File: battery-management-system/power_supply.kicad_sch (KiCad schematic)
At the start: 39 parts, among them J14 VIN, J24 3V3, J25 5V, J26 5V, U1 L6982C33DR, U12 MIC2250-1YD5, U2 L6982C33DR

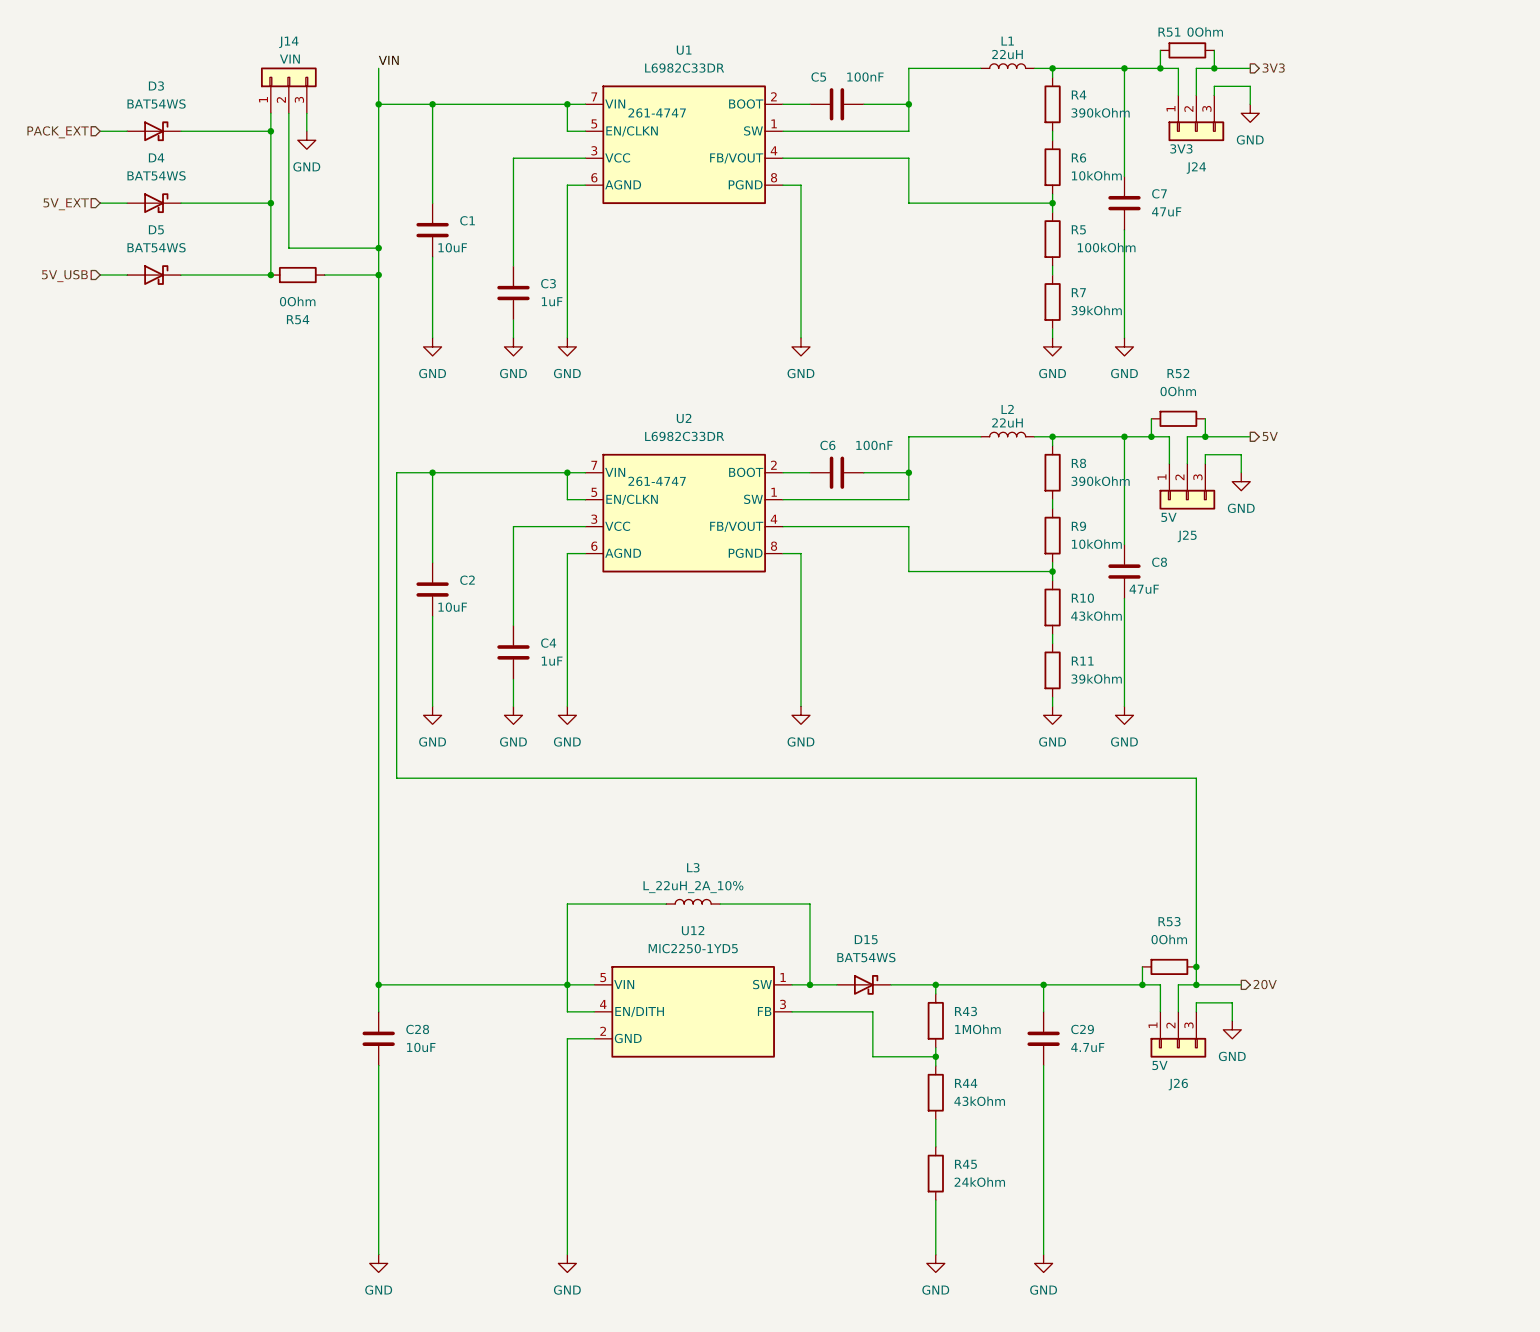
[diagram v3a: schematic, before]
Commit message: fix current sensing
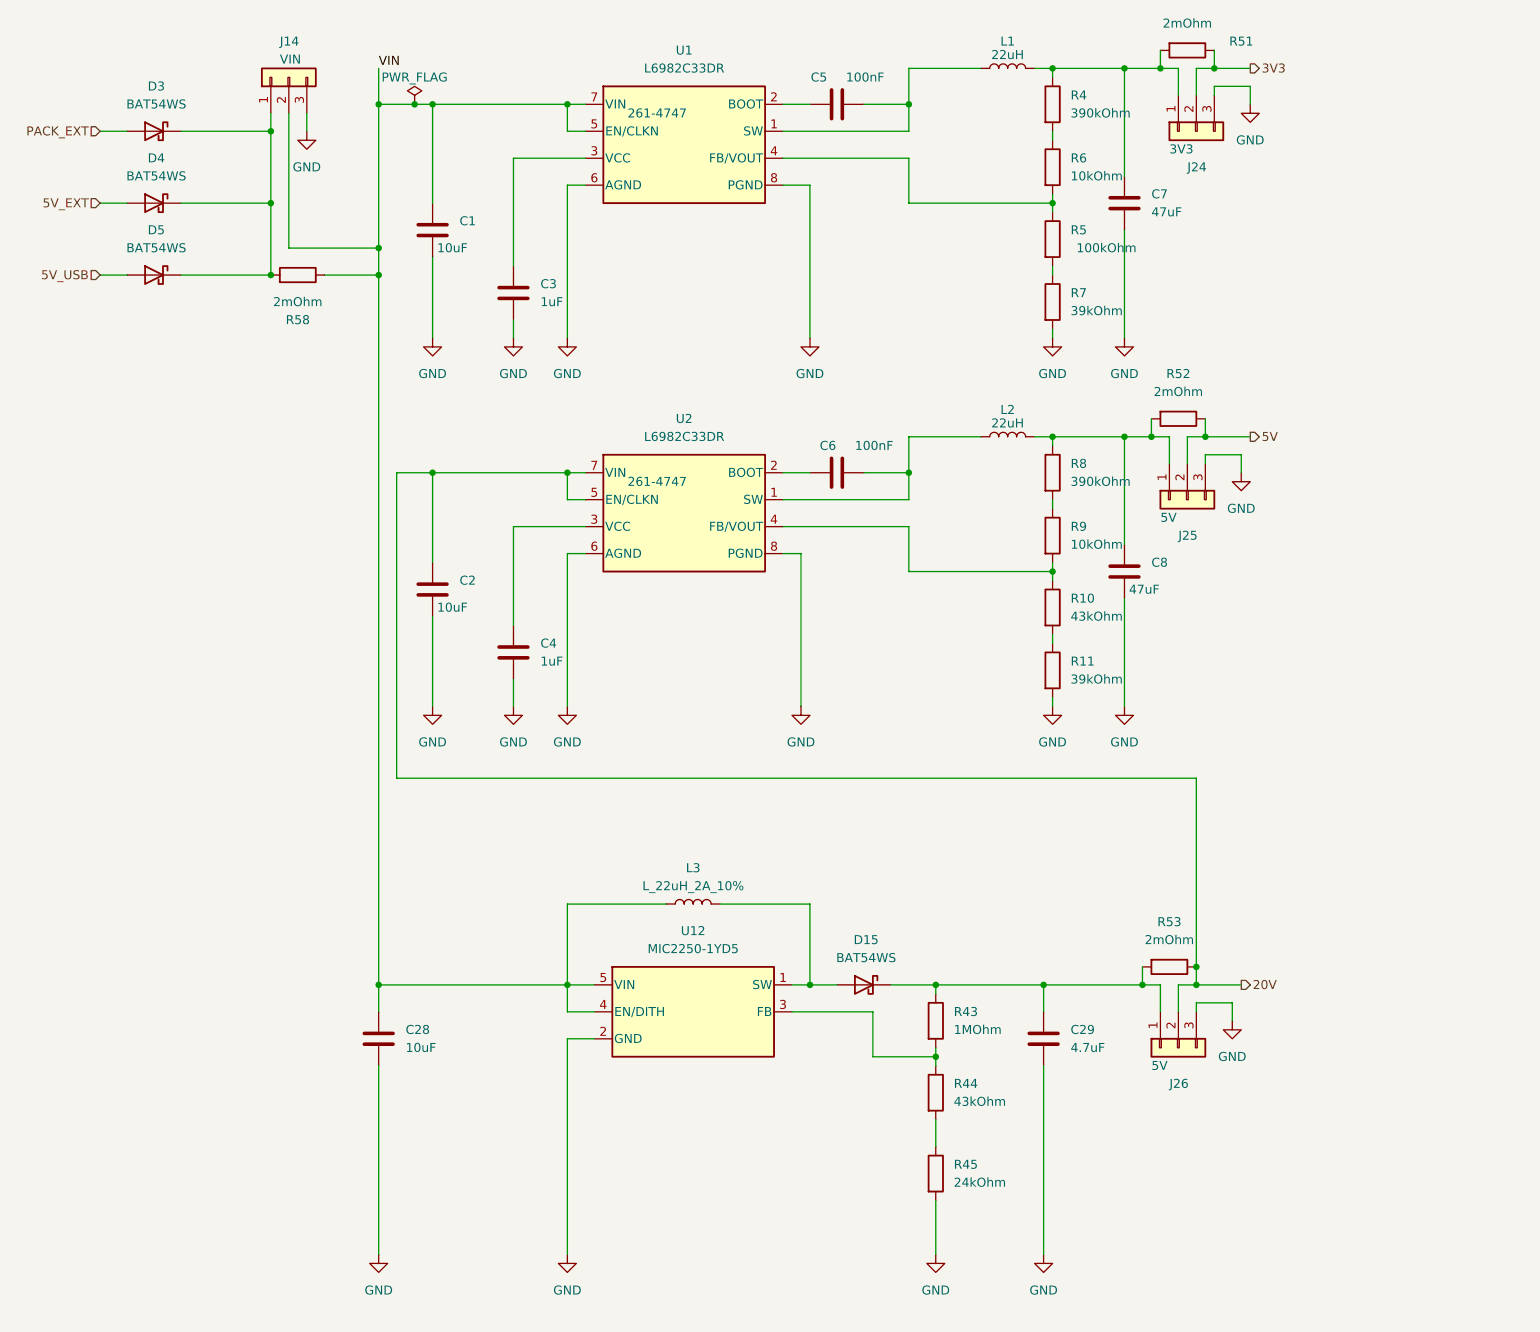
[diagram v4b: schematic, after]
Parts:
- removed R51, R52, R53, R54: 0Ohm, benediktibk:R_0603_1608Metric_Pad0.98x0.95mm_HandSolder, symbol benediktibk:R_0Ohm_SMD_0603_100mW_0%
- added R51, R52, R53, R58: 2mOhm, benediktibk:R_2512_6332Metric_Pad1.40x3.35mm_HandSolder, symbol benediktibk:R_2mOhm_SMD_2512_5W_1%
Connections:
- net 20V: now also R53.1
- net 3V3: now also R51.1
- net 5V: now also R52.1
- net VIN: now also R58.1
- net at C7.1, J24.1 (Pin_1), L1.1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: now also R51.2
- net at C8.1, J25.1 (Pin_1), L2.1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: now also R52.2
- net at C29.1, D15.1 (K), J26.1 (Pin_1)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: now also R53.2
- net at D3.1 (K), D4.1 (K), D5.1 (K)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: now also R58.2

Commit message: add negative power supply for OPAMPs
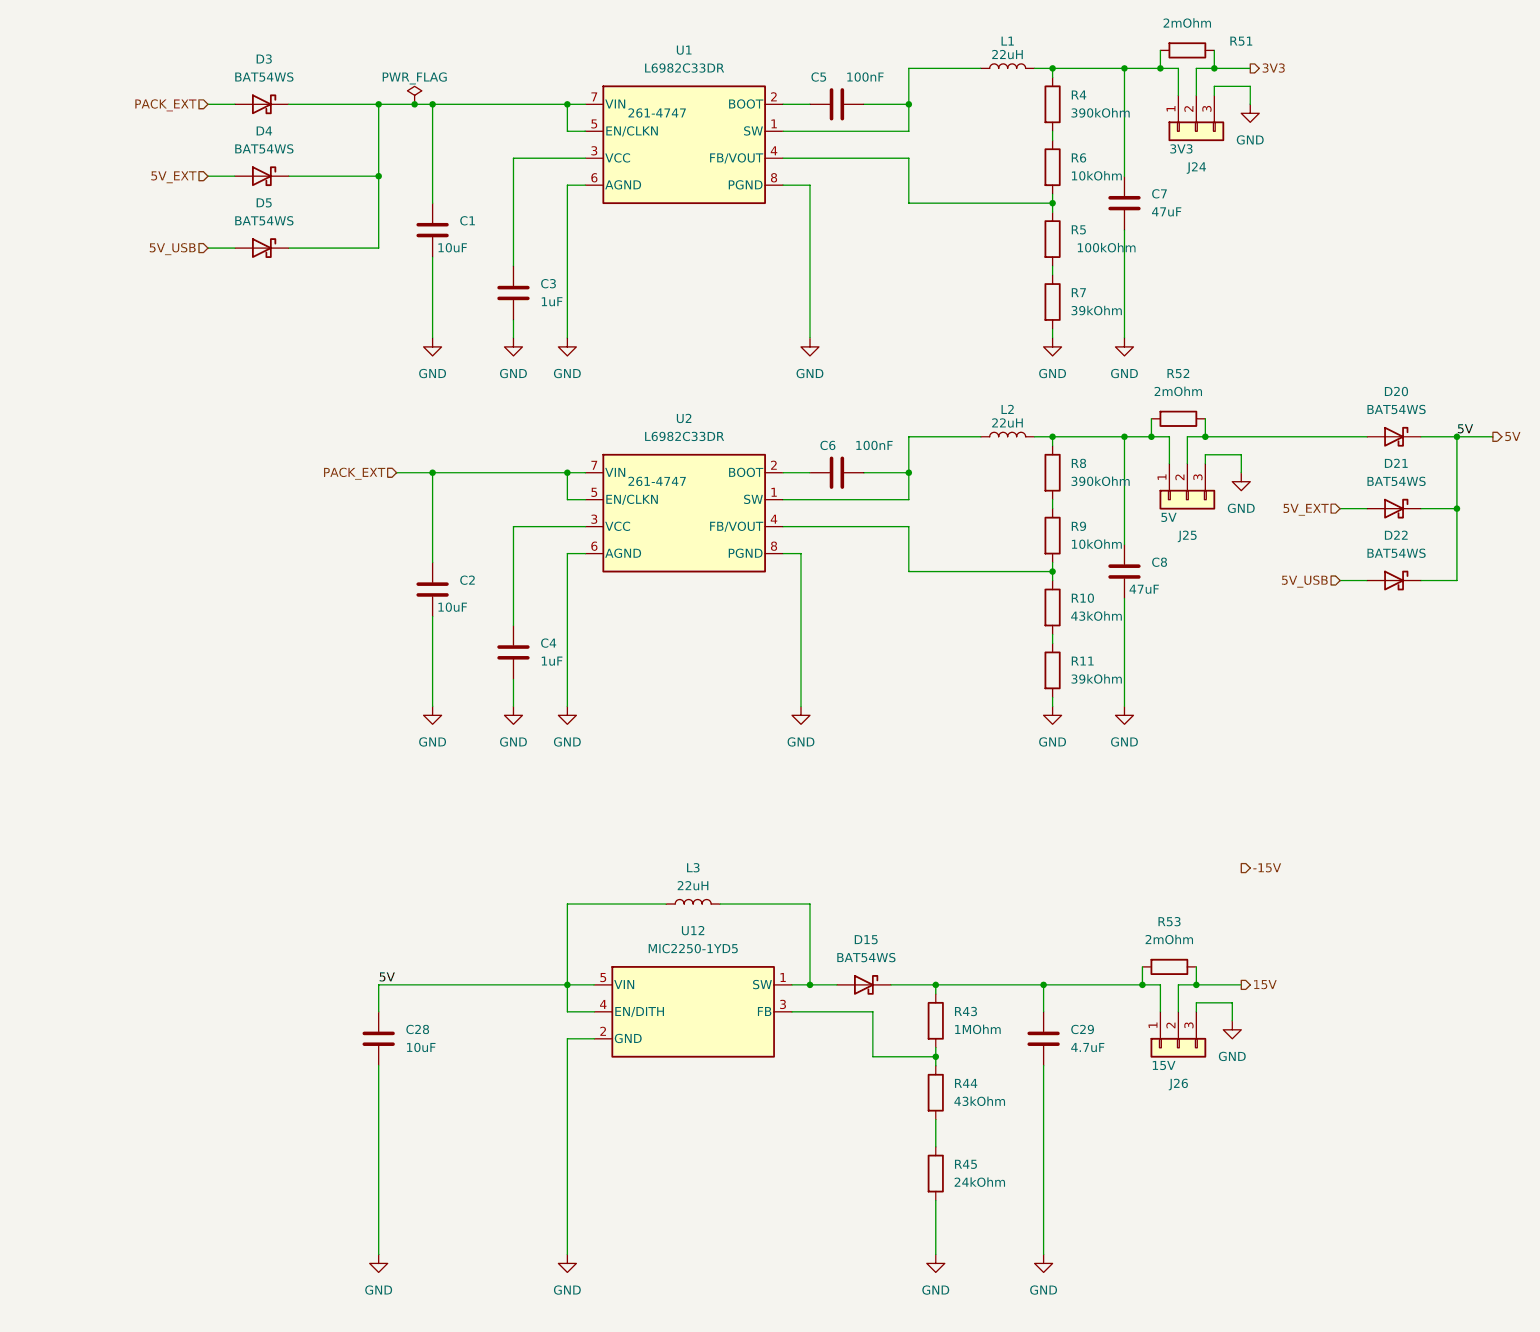
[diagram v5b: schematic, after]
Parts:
- removed J14: VIN, benediktibk:PinHeader_1x03_P2.54mm_Vertical, symbol benediktibk:Conn_01x03
- removed R58: 2mOhm, benediktibk:R_2512_6332Metric_Pad1.40x3.35mm_HandSolder, symbol benediktibk:R_2mOhm_SMD_2512_5W_1%
- added D20, D21, D22: BAT54WS, benediktibk:D_SOD-323, symbol benediktibk:BAT54WS
- J26: value 5V -> 15V
- L3: value L_22uH_2A_10% -> 22uH
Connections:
- net 5V: now also C28.1, L3.1, U12.4 (EN/DITH), U12.5 (VIN), D20.1 (K), D21.1 (K), D22.1 (K); no longer J25.2 (Pin_2), R52.1
- net 5V_EXT: now also D21.2 (A)
- net 5V_USB: now also D22.2 (A)
- net PACK_EXT: now also C2.1, U2.5 (EN/CLKN), U2.7 (VIN)
- net at D3.1 (K), D4.1 (K), D5.1 (K): now also C1.1, U1.5 (EN/CLKN), U1.7 (VIN)
- removed net 20V: C2.1, J26.2 (Pin_2), R53.1, U2.5 (EN/CLKN), U2.7 (VIN)
- removed net VIN: C1.1, C28.1, L3.1, U1.5 (EN/CLKN), U1.7 (VIN), U12.4 (EN/DITH), U12.5 (VIN)
- new net: D20.2 (A), J25.2 (Pin_2), R52.1
- new net 15V: J26.2 (Pin_2), R53.1
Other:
- moved on the sheet: D3, D4, D5

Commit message: implement negative power supply for OPAMPs
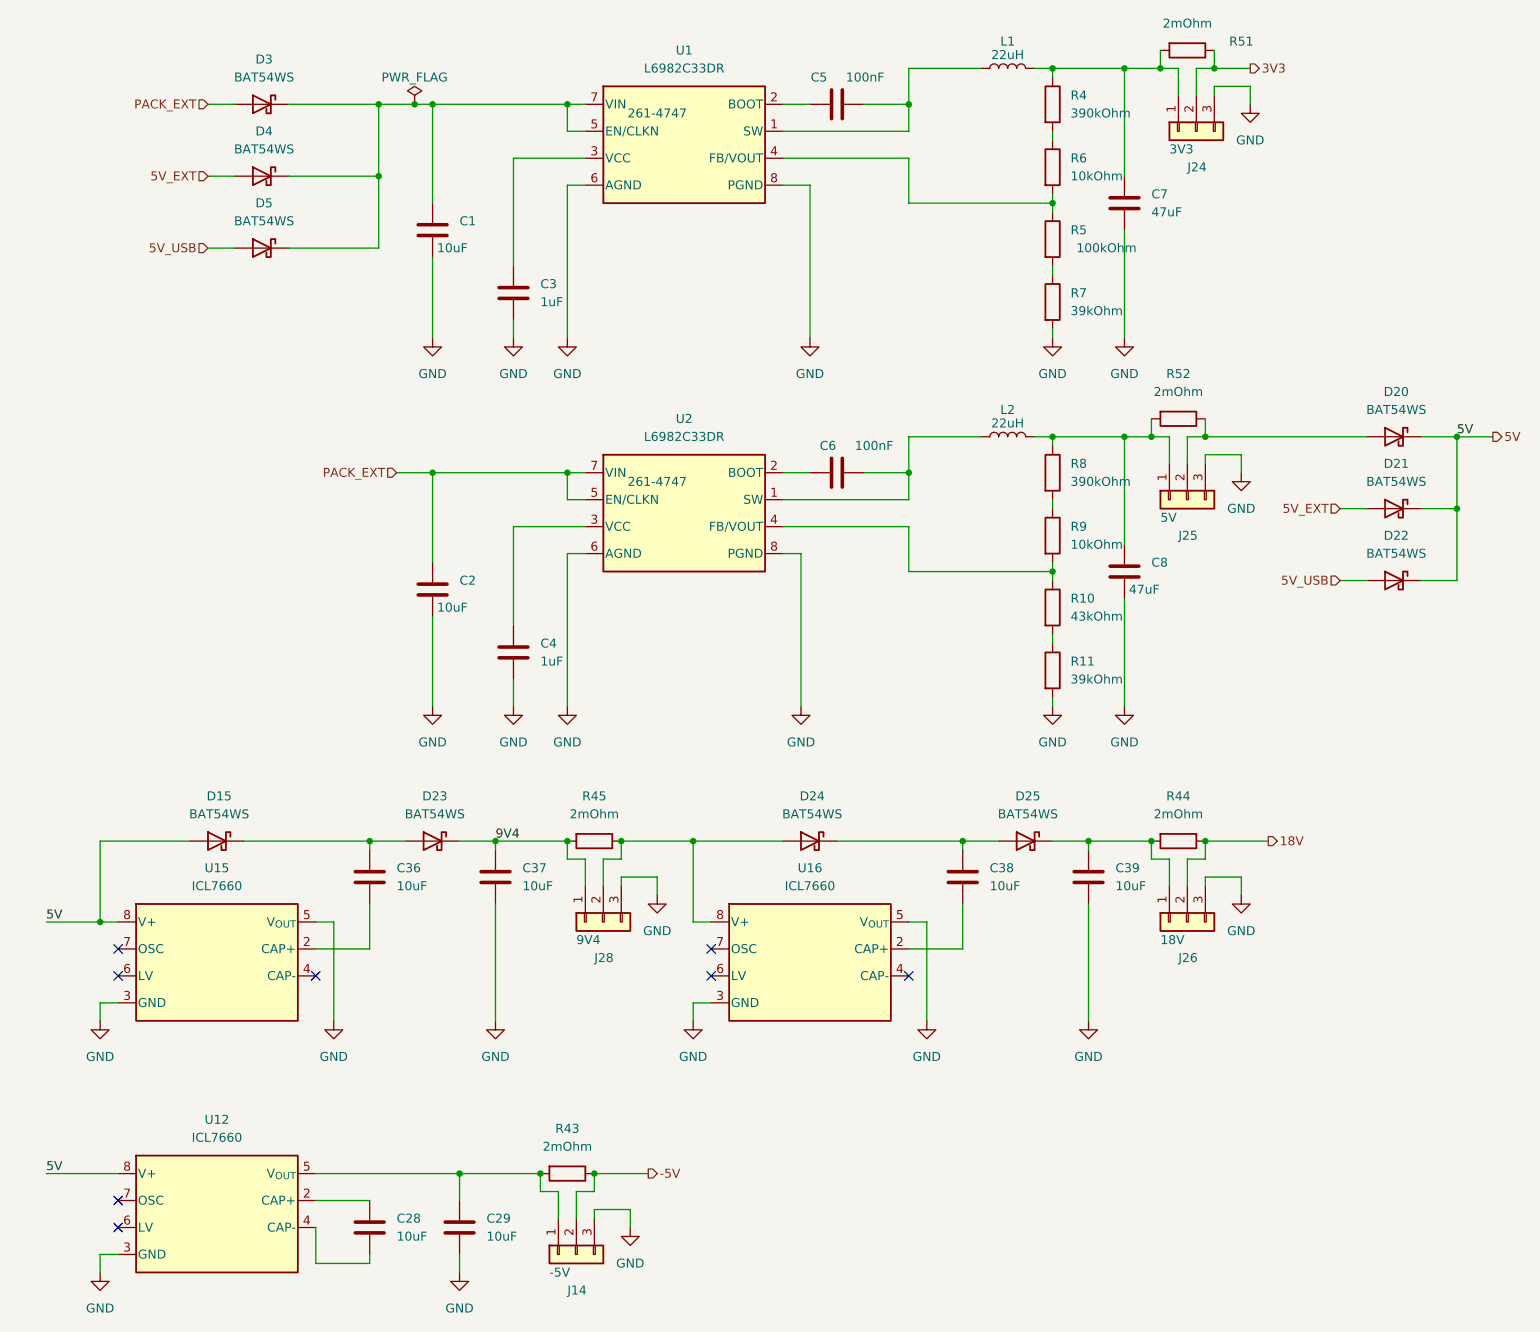
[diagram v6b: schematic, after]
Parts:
- removed C29: 4.7uF, benediktibk:C_0805_2012Metric_Pad1.18x1.45mm_HandSolder, symbol benediktibk:C_4_7uF_SMD_0805_50V_10%
- removed L3: 22uH, benediktibk:L_Radial_D9.5mm_P5.00mm_Fastron_07HVP, symbol benediktibk:L_22uH_2A_10%
- removed R43: 1MOhm, benediktibk:R_0603_1608Metric_Pad0.98x0.95mm_HandSolder, symbol benediktibk:R_1MOhm_SMD_0603_100mW_1%
- removed R44: 43kOhm, benediktibk:R_0603_1608Metric_Pad0.98x0.95mm_HandSolder, symbol benediktibk:R_43kOhm_SMD_0603_100mW_1%
- removed R45: 24kOhm, benediktibk:R_0603_1608Metric_Pad0.98x0.95mm_HandSolder, symbol benediktibk:R_24kOhm_SMD_0603_100mW_1%
- removed R53: 2mOhm, benediktibk:R_2512_6332Metric_Pad1.40x3.35mm_HandSolder, symbol benediktibk:R_2mOhm_SMD_2512_5W_1%
- removed U12: MIC2250-1YD5, benediktibk:SOT-23-5, symbol benediktibk:MIC2250-1YD5
- added C29, C36, C37, C38, C39: 10uF, benediktibk:C_1210_3225Metric_Pad1.33x2.70mm_HandSolder, symbol benediktibk:C_10uF_SMD_1210_50V_20%
- added D23, D24, D25: BAT54WS, benediktibk:D_SOD-323, symbol benediktibk:BAT54WS
- added J14: -5V, benediktibk:PinHeader_1x03_P2.54mm_Vertical, symbol benediktibk:Conn_01x03
- added J28: 9V4, benediktibk:PinHeader_1x03_P2.54mm_Vertical, symbol benediktibk:Conn_01x03
- added R43, R44, R45: 2mOhm, benediktibk:R_2512_6332Metric_Pad1.40x3.35mm_HandSolder, symbol benediktibk:R_2mOhm_SMD_2512_5W_1%
- added U12, U15, U16: ICL7660, benediktibk:SOIC-8_3.9x4.9mm_P1.27mm, symbol benediktibk:ICL7660
- J26: value 15V -> 18V
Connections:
- net 5V: now also D15.2 (A), U12.8 (V+), U15.8 (V+); no longer C28.1
- net GND: now also C29.2, C37.2, C39.2, J14.3 (Pin_3), J28.3 (Pin_3), U12.3 (GND), U15.3 (GND), U15.5 (V_{OUT}), U16.3 (GND), U16.5 (V_{OUT}); no longer C28.2
- net at D15.1 (K): now also C36.1, D23.2 (A); no longer J26.1 (Pin_1)
- net 15V renamed 18V
- net 18V: now also R44.1
- new net: C29.1, J14.1 (Pin_1), R43.2, U12.5 (V_{OUT})
- new net: C38.1, D24.1 (K), D25.2 (A)
- new net: D24.2 (A), J28.2 (Pin_2), R45.1, U16.8 (V+)
- new net: C36.2, U15.2 (CAP+)
- new net: C39.1, D25.1 (K), J26.1 (Pin_1), R44.2
- new net: C38.2, U16.2 (CAP+)
- new net: C28.1, U12.2 (CAP+)
- new net: C28.2, U12.4 (CAP-)
- new net -5V: J14.2 (Pin_2), R43.1
- new net 9V4: C37.1, D23.1 (K), J28.1 (Pin_1), R45.2
- no-connect marks 0 -> 8
